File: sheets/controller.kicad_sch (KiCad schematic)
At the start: 44 parts, among them CN1 CTRL1, CN2 CTRL2, U12 74LS06

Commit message: Resistor Value Ω added
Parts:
- R22, R23, R24, R25, R26, R27: value 22 -> 22Ω
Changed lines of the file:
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@@
     (in_bom yes) (on_board yes)
     (property "Reference" "R26" (id 0) (at 262.89 196.85 90))
-    (property "Value" "22" (id 1) (at 262.89 200.914 90))
+    (property "Value" "22Ω" (id 1) (at 262.89 200.914 90))
     (property "Footprint" "" (id 2) (at 262.89 198.882 0)
       (effects (font (size 1.27 1.27)) hide)
@@
     (in_bom yes) (on_board yes)
     (property "Reference" "R27" (id 0) (at 262.89 182.372 90))
-    (property "Value" "22" (id 1) (at 262.89 186.436 90))
+    (property "Value" "22Ω" (id 1) (at 262.89 186.436 90))
     (property "Footprint" "" (id 2) (at 262.89 184.404 0)
       (effects (font (size 1.27 1.27)) hide)
@@
     (in_bom yes) (on_board yes)
     (property "Reference" "R23" (id 0) (at 262.89 111.76 90))
-    (property "Value" "22" (id 1) (at 262.89 115.824 90))
+    (property "Value" "22Ω" (id 1) (at 262.89 115.824 90))
     (property "Footprint" "" (id 2) (at 262.89 113.792 0)
       (effects (font (size 1.27 1.27)) hide)
@@
     (in_bom yes) (on_board yes)
     (property "Reference" "R25" (id 0) (at 262.89 211.328 90))
-    (property "Value" "22" (id 1) (at 262.89 215.392 90))
+    (property "Value" "22Ω" (id 1) (at 262.89 215.392 90))
     (property "Footprint" "" (id 2) (at 262.89 213.36 0)
       (effects (font (size 1.27 1.27)) hide)
@@
     (in_bom yes) (on_board yes)
     (property "Reference" "R24" (id 0) (at 262.89 97.282 90))
-    (property "Value" "22" (id 1) (at 262.89 101.346 90))
+    (property "Value" "22Ω" (id 1) (at 262.89 101.346 90))
     (property "Footprint" "" (id 2) (at 262.89 99.314 0)
       (effects (font (size 1.27 1.27)) hide)
@@
     (in_bom yes) (on_board yes)
     (property "Reference" "R22" (id 0) (at 262.89 126.238 90))
-    (property "Value" "22" (id 1) (at 262.89 130.302 90))
+    (property "Value" "22Ω" (id 1) (at 262.89 130.302 90))
     (property "Footprint" "" (id 2) (at 262.89 128.27 0)
       (effects (font (size 1.27 1.27)) hide)

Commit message: Assigning Footprints
Assigned some footprints to some components. Can still be wrong size on caps
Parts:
- BF1, BF10, BF11, BF12, BF13, BF14, BF15, BF16, BF17, BF18, BF19, BF2, BF20, BF21, BF22, BF23, BF24, BF25, BF26, BF27, BF28, BF29, BF3, BF30, BF4, BF5, BF6, BF7, BF8, BF9: footprint (none) -> 1_NeoGeoLibrary:BF-2.5mm
- R22, R23, R24, R25, R26, R27: footprint (none) -> 1_NeoGeoLibrary:Resistor1-5mm

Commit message: Updated Footprints
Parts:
- CN1, CN2: footprint (none) -> Connector_Dsub:DSUB-15_Male_Horizontal_P2.77x2.84mm_EdgePinOffset14.56mm_Housed_MountingHolesOffset15.98mm
- U12: footprint (none) -> Package_DIP:DIP-14_W7.62mm
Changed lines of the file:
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@@
     (property "Reference" "U12" (id 0) (at 243.586 124.206 0))
     (property "Value" "74LS06" (id 1) (at 243.586 133.096 0))
-    (property "Footprint" "" (id 2) (at 243.586 128.27 0)
+    (property "Footprint" "Package_DIP:DIP-14_W7.62mm" (id 2) (at 243.586 128.27 0)
       (effects (font (size 1.27 1.27)) hide)
     )
@@
     (property "Reference" "U12" (id 0) (at 243.586 209.296 0))
     (property "Value" "74LS06" (id 1) (at 243.586 218.186 0))
-    (property "Footprint" "" (id 2) (at 243.586 213.36 0)
+    (property "Footprint" "Package_DIP:DIP-14_W7.62mm" (id 2) (at 243.586 213.36 0)
       (effects (font (size 1.27 1.27)) hide)
     )
@@
     (property "Reference" "CN1" (id 0) (at 318.77 56.388 0))
     (property "Value" "CTRL1" (id 1) (at 318.77 99.06 0))
-    (property "Footprint" "" (id 2) (at 318.77 77.47 0)
+    (property "Footprint" "Connector_Dsub:DSUB-15_Male_Horizontal_P2.77x2.84mm_EdgePinOffset14.56mm_Housed_MountingHolesOffset15.98mm" (id 2) (at 318.77 77.47 0)
       (effects (font (size 1.27 1.27)) hide)
     )
@@
     (property "Reference" "CN2" (id 0) (at 318.77 141.478 0))
     (property "Value" "CTRL2" (id 1) (at 318.77 184.15 0))
-    (property "Footprint" "" (id 2) (at 318.77 162.56 0)
+    (property "Footprint" "Connector_Dsub:DSUB-15_Male_Horizontal_P2.77x2.84mm_EdgePinOffset14.56mm_Housed_MountingHolesOffset15.98mm" (id 2) (at 318.77 162.56 0)
       (effects (font (size 1.27 1.27)) hide)
     )
@@
     (property "Reference" "U12" (id 0) (at 243.586 94.996 0))
     (property "Value" "74LS06" (id 1) (at 243.586 104.14 0))
-    (property "Footprint" "" (id 2) (at 243.586 99.314 0)
+    (property "Footprint" "Package_DIP:DIP-14_W7.62mm" (id 2) (at 243.586 99.314 0)
       (effects (font (size 1.27 1.27)) hide)
     )
@@
     (property "Reference" "U12" (id 0) (at 243.586 109.728 0))
     (property "Value" "74LS06" (id 1) (at 243.586 118.618 0))
-    (property "Footprint" "" (id 2) (at 243.586 113.792 0)
+    (property "Footprint" "Package_DIP:DIP-14_W7.62mm" (id 2) (at 243.586 113.792 0)
       (effects (font (size 1.27 1.27)) hide)
     )
@@
     (property "Reference" "U12" (id 0) (at 243.586 180.34 0))
     (property "Value" "74LS06" (id 1) (at 243.586 189.23 0))
-    (property "Footprint" "" (id 2) (at 243.586 184.404 0)
+    (property "Footprint" "Package_DIP:DIP-14_W7.62mm" (id 2) (at 243.586 184.404 0)
       (effects (font (size 1.27 1.27)) hide)
     )
@@
     (property "Reference" "U12" (id 0) (at 243.586 194.818 0))
     (property "Value" "74LS06" (id 1) (at 243.586 203.708 0))
-    (property "Footprint" "" (id 2) (at 243.586 198.882 0)
-      (effects (font (size 1.27 1.27)) hide)
-    )
+    (property "Footprint" "Package_DIP:DIP-14_W7.62mm" (id 2) (at 243.586 198.882 0)
+      (effects (font (size 1.27 1.27)) hide)
+    )

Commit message: U12 OUT21 and OUT23 wrong way on original schematic Added Cap on RESETP Pin20 Neo-D0
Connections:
- net OUT21: now also U12.9; no longer U12.13
- net OUT23: now also U12.13; no longer U12.9
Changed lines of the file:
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@@
     )
   )
-  (global_label "OUT21" (shape input) (at 235.966 184.404 180) (fields_autoplaced)
+  (global_label "OUT21" (shape input) (at 235.966 213.36 180) (fields_autoplaced)
     (effects (font (size 1.27 1.27)) (justify right))
-    (property "Intersheet References" "${INTERSHEET_REFS}" (id 0) (at 227.5053 184.3246 0)
+    (property "Intersheet References" "${INTERSHEET_REFS}" (id 0) (at 227.5053 213.2806 0)
       (effects (font (size 1.27 1.27)) (justify right) hide)
     )
@@
     )
   )
-  (global_label "OUT23" (shape input) (at 235.966 213.36 180) (fields_autoplaced)
+  (global_label "OUT23" (shape input) (at 235.966 184.404 180) (fields_autoplaced)
     (effects (font (size 1.27 1.27)) (justify right))
-    (property "Intersheet References" "${INTERSHEET_REFS}" (id 0) (at 227.5053 213.2806 0)
+    (property "Intersheet References" "${INTERSHEET_REFS}" (id 0) (at 227.5053 184.3246 0)
       (effects (font (size 1.27 1.27)) (justify right) hide)
     )

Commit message: Fix Wrong Component for Resistors on Controller Port 1 and 2. Changed to Resistor Array SIP
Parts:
- removed R22, R23, R24, R25, R26, R27: 22Ω, 1_NeoGeoLibrary:Resistor1-5mm, symbol Device:R_Small
- added RN1, RN2: 22Ω, Resistor_THT:R_Array_SIP8, symbol Device:R_Pack04_SIP_Split
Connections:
- net at U12.2: now also RN1.2 (R1.2)
- net at U12.10: now also RN2.4 (R2.2)
- net at BF25.1: now also RN2.3 (R2.1)
- net at BF21.1: now also RN1.1 (R1.1)
- net at U12.8: now also RN2.6 (R3.2)
- net at U12.12: now also RN2.2 (R1.2)
- net at BF24.1: now also RN2.1 (R1.1)
- net at U12.4: now also RN1.4 (R2.2)
- net at BF22.1: now also RN1.3 (R2.1)
- net at BF26.1: now also RN2.5 (R3.1)
- net at U12.6: now also RN1.6 (R3.2)
- net at BF23.1: now also RN1.5 (R3.1)

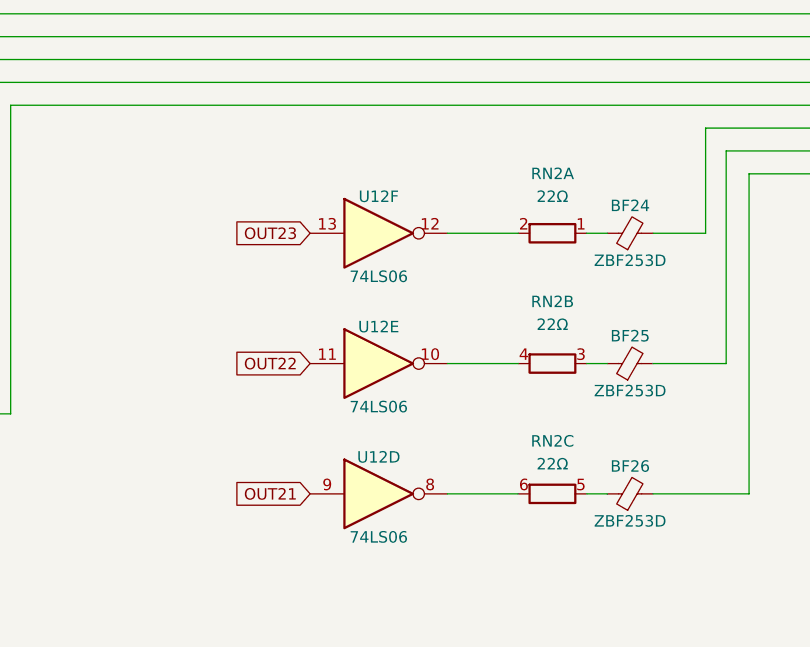
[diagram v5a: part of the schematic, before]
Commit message: Fix Wrong LS06 connection to CN2 on the 22X4 (RN2)
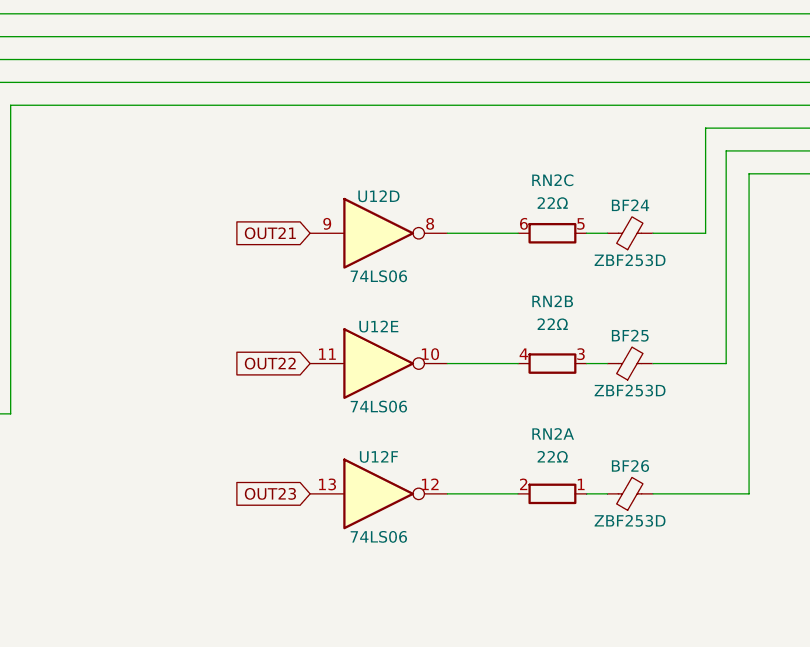
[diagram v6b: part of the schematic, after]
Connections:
- net at RN2.5 (R3.1): now also BF24.1; no longer BF26.1
- net at RN2.1 (R1.1): now also BF26.1; no longer BF24.1
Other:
- moved on the sheet: RN2A, RN2C, U12D, U12F

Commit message: Sync footprints from Nightly Build
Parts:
- CN1, CN2: footprint Connector_Dsub:DSUB-15_Male_Horizontal_P2.77x2.84mm_EdgePinOffset14.56mm_Housed_MountingHolesOffset15.98mm -> 1_NeoGeoLibrary:CN1-2
- CR1, CR2, CR3, CR4, CR5: footprint Package_DIP:DIP-28_W15.24mm -> Resistor_THT:R_Array_SIP10
- RN1, RN2: footprint Resistor_THT:R_Array_SIP8 -> 1_NeoGeoLibrary:RN2
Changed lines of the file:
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@@
     (property "Reference" "CR2" (id 0) (at 103.378 162.814 0))
     (property "Value" "CRE401" (id 1) (at 105.41 182.88 0))
-    (property "Footprint" "Package_DIP:DIP-28_W15.24mm" (id 2) (at 109.474 189.23 0)
+    (property "Footprint" "Resistor_THT:R_Array_SIP10" (id 2) (at 109.474 189.23 0)
       (effects (font (size 1.27 1.27)) hide)
     )
@@
     (property "Reference" "RN2" (id 0) (at 262.89 178.562 90))
     (property "Value" "22Ω" (id 1) (at 262.89 181.102 90))
-    (property "Footprint" "Resistor_THT:R_Array_SIP8" (id 2) (at 262.89 186.436 90)
+    (property "Footprint" "1_NeoGeoLibrary:RN2" (id 2) (at 262.89 186.436 90)
       (effects (font (size 1.27 1.27)) hide)
     )
@@
     (property "Reference" "RN1" (id 0) (at 262.89 122.428 90))
     (property "Value" "22Ω" (id 1) (at 262.89 124.968 90))
-    (property "Footprint" "Resistor_THT:R_Array_SIP8" (id 2) (at 262.89 130.302 90)
+    (property "Footprint" "1_NeoGeoLibrary:RN2" (id 2) (at 262.89 130.302 90)
       (effects (font (size 1.27 1.27)) hide)
     )
@@
     (property "Reference" "CR3" (id 0) (at 103.378 136.144 0))
     (property "Value" "CRE401" (id 1) (at 105.41 156.21 0))
-    (property "Footprint" "Package_DIP:DIP-28_W15.24mm" (id 2) (at 109.474 162.56 0)
+    (property "Footprint" "Resistor_THT:R_Array_SIP10" (id 2) (at 109.474 162.56 0)
       (effects (font (size 1.27 1.27)) hide)
     )
@@
     (property "Reference" "CN1" (id 0) (at 318.77 56.388 0))
     (property "Value" "CTRL1" (id 1) (at 318.77 99.06 0))
-    (property "Footprint" "Connector_Dsub:DSUB-15_Male_Horizontal_P2.77x2.84mm_EdgePinOffset14.56mm_Housed_MountingHolesOffset15.98mm" (id 2) (at 318.77 77.47 0)
+    (property "Footprint" "1_NeoGeoLibrary:CN1-2" (id 2) (at 318.77 77.47 0)
       (effects (font (size 1.27 1.27)) hide)
     )
@@
     (property "Reference" "CR1" (id 0) (at 103.378 189.484 0))
     (property "Value" "CRE401" (id 1) (at 105.41 209.55 0))
-    (property "Footprint" "Package_DIP:DIP-28_W15.24mm" (id 2) (at 109.474 215.9 0)
+    (property "Footprint" "Resistor_THT:R_Array_SIP10" (id 2) (at 109.474 215.9 0)
       (effects (font (size 1.27 1.27)) hide)
     )
@@
     (property "Reference" "RN2" (id 0) (at 262.89 206.756 90))
     (property "Value" "22Ω" (id 1) (at 262.89 209.296 90))
-    (property "Footprint" "Resistor_THT:R_Array_SIP8" (id 2) (at 262.89 215.392 90)
+    (property "Footprint" "1_NeoGeoLibrary:RN2" (id 2) (at 262.89 215.392 90)
       (effects (font (size 1.27 1.27)) hide)
     )
@@
     (property "Reference" "RN1" (id 0) (at 262.89 92.964 90))
     (property "Value" "22Ω" (id 1) (at 262.89 95.504 90))
-    (property "Footprint" "Resistor_THT:R_Array_SIP8" (id 2) (at 262.89 101.346 90)
+    (property "Footprint" "1_NeoGeoLibrary:RN2" (id 2) (at 262.89 101.346 90)
       (effects (font (size 1.27 1.27)) hide)
     )
@@
     (property "Reference" "CN2" (id 0) (at 318.77 141.478 0))
     (property "Value" "CTRL2" (id 1) (at 318.77 184.15 0))
-    (property "Footprint" "Connector_Dsub:DSUB-15_Male_Horizontal_P2.77x2.84mm_EdgePinOffset14.56mm_Housed_MountingHolesOffset15.98mm" (id 2) (at 318.77 162.56 0)
+    (property "Footprint" "1_NeoGeoLibrary:CN1-2" (id 2) (at 318.77 162.56 0)
       (effects (font (size 1.27 1.27)) hide)
     )
@@
     (property "Reference" "RN1" (id 0) (at 262.89 107.95 90))
     (property "Value" "22Ω" (id 1) (at 262.89 110.49 90))
-    (property "Footprint" "Resistor_THT:R_Array_SIP8" (id 2) (at 262.89 115.824 90)
+    (property "Footprint" "1_NeoGeoLibrary:RN2" (id 2) (at 262.89 115.824 90)
       (effects (font (size 1.27 1.27)) hide)
     )
@@
     (property "Reference" "RN2" (id 0) (at 262.89 192.024 90))
     (property "Value" "22Ω" (id 1) (at 262.89 194.564 90))
-    (property "Footprint" "Resistor_THT:R_Array_SIP8" (id 2) (at 262.89 200.914 90)
+    (property "Footprint" "1_NeoGeoLibrary:RN2" (id 2) (at 262.89 200.914 90)
       (effects (font (size 1.27 1.27)) hide)
     )
@@
     (property "Reference" "CR5" (id 0) (at 103.378 56.134 0))
     (property "Value" "CRE401" (id 1) (at 105.41 76.2 0))
-    (property "Footprint" "Package_DIP:DIP-28_W15.24mm" (id 2) (at 109.474 82.55 0)
+    (property "Footprint" "Resistor_THT:R_Array_SIP10" (id 2) (at 109.474 82.55 0)
       (effects (font (size 1.27 1.27)) hide)
     )
@@
     (property "Reference" "CR4" (id 0) (at 103.378 82.804 0))
     (property "Value" "CRE401" (id 1) (at 105.41 102.87 0))
-    (property "Footprint" "Package_DIP:DIP-28_W15.24mm" (id 2) (at 109.474 109.22 0)
-      (effects (font (size 1.27 1.27)) hide)
-    )
+    (property "Footprint" "Resistor_THT:R_Array_SIP10" (id 2) (at 109.474 109.22 0)
+      (effects (font (size 1.27 1.27)) hide)
+    )

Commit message: Upgrade Schematics to Kicad 7.0
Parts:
- CN1, CN2: symbol Connector:DB15_Male -> Connector:DA15_Plug
